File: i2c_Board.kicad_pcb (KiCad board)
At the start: 2 copper layers, 47.3 x 38 mm, 23 parts, among them J1 Conn_01x09_Pin, J2 Logic Analyzer Connector Pins, U1 MCP9808, U2 MCP7940N, Y1 Crystal

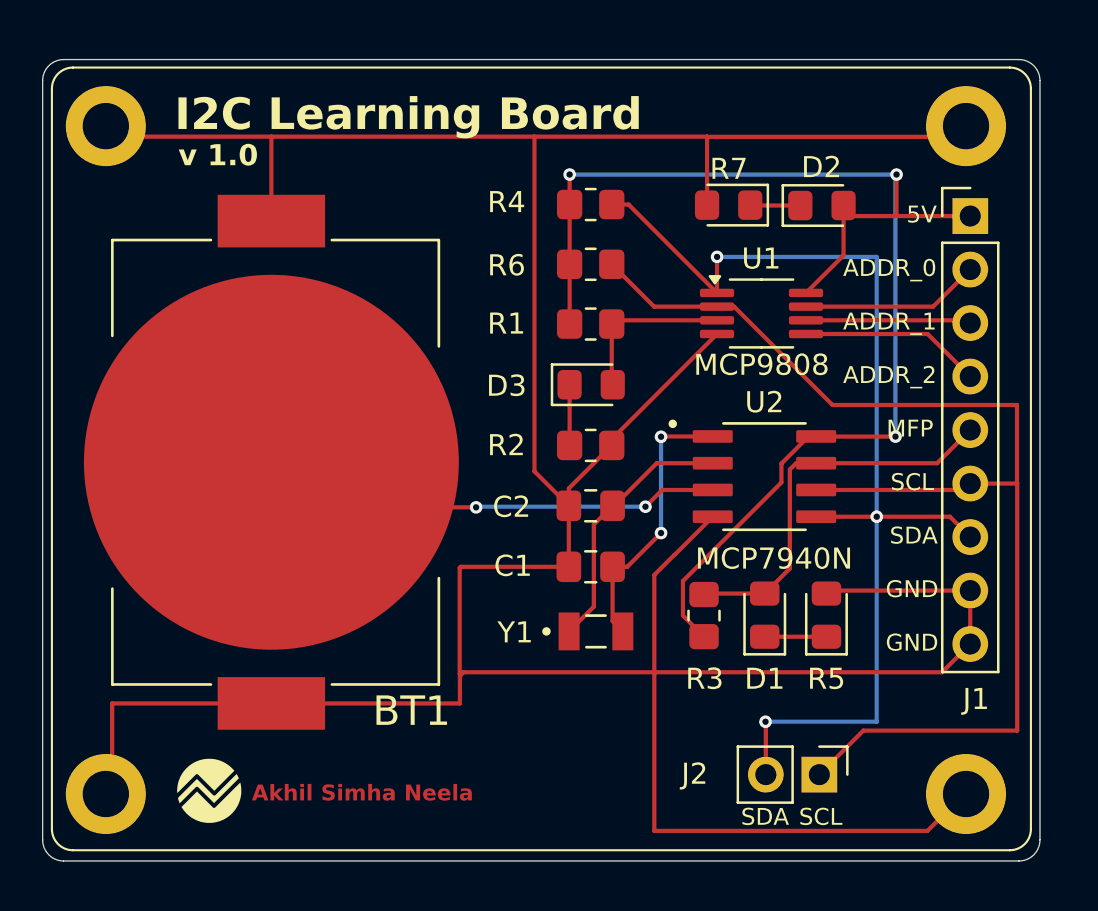
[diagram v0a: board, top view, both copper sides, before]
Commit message: Modified footprint & Rearranged routing
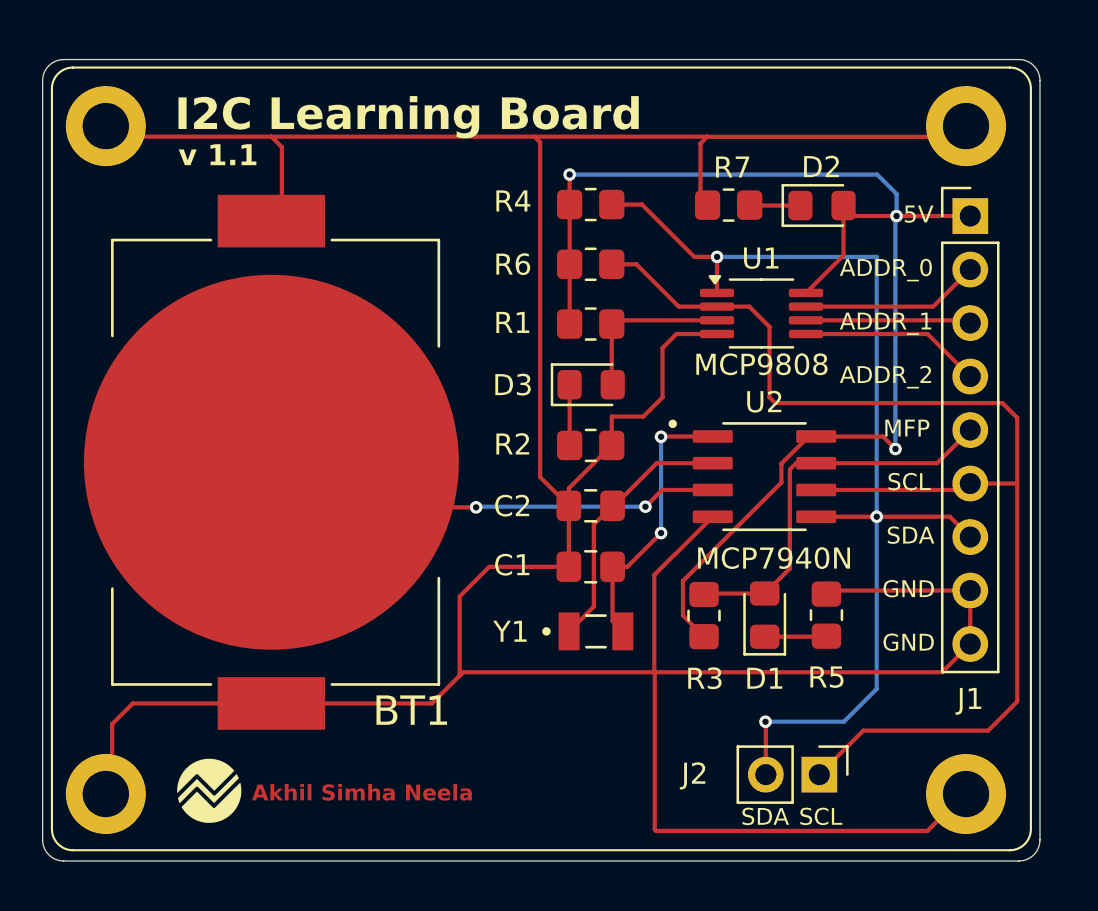
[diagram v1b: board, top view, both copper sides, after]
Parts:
- R5, R7: footprint Diode_SMD:D_0805_2012Metric_Pad1.15x1.40mm_HandSolder -> Resistor_SMD:R_0805_2012Metric_Pad1.20x1.40mm_HandSolder
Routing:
- net +5V: track 64.7 -> 63.0 mm
- net MCU_SDA: track 53.6 -> 52.0 mm
- net MCU_SCL: track 57.4 -> 58.2 mm
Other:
- board text added: "v 1.1"
- board text removed: "v 1.0"

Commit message: Changed Capacitor value from 6nF to 6pF
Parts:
- C1, C2: value 6n -> 6p
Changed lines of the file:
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@@
 			)
 		)
-		(property "Value" "6n"
+		(property "Value" "6p"
 			(at 0 1.68 0)
 			(layer "F.Fab")
@@
 			)
 		)
-		(property "Value" "6n"
+		(property "Value" "6p"
 			(at 0 1.68 0)
 			(layer "F.Fab")

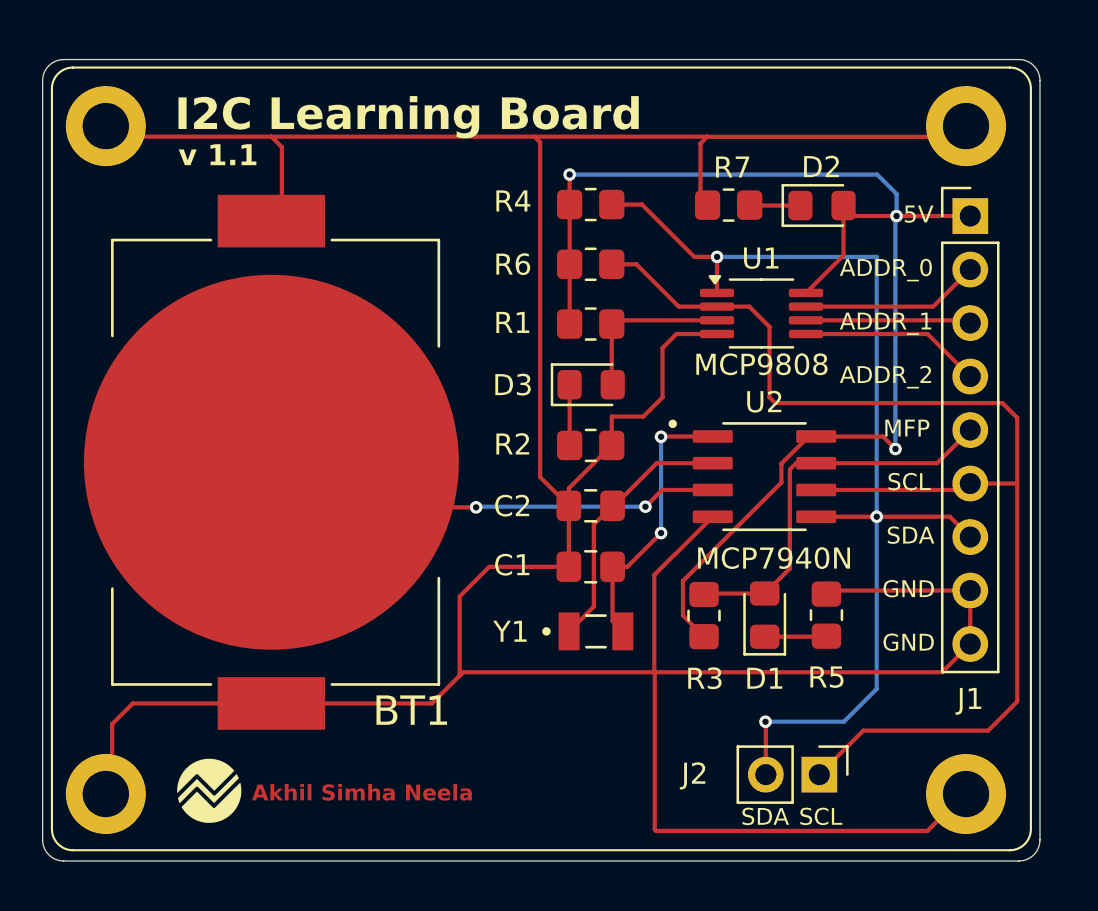
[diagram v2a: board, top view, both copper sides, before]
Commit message: Optimised board to smaller size & Added Ground Plane
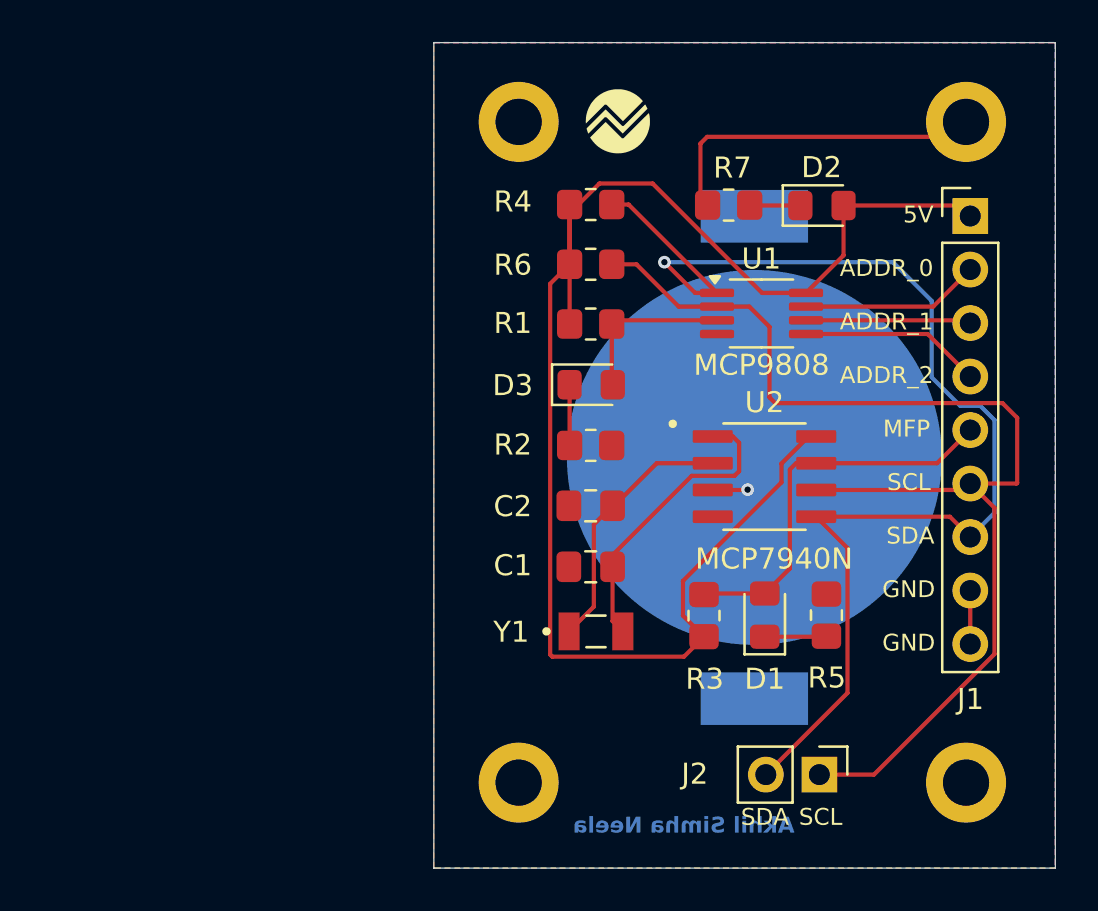
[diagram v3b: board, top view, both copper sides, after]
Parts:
- BT1: moved to B.Cu
- moved G*** 37.2 mm to (146.5, 75.9)
- moved BT1 22.9 mm to (152.9, 91.9)
- moved H4 19.6 mm to (141.8, 107.3)
- moved H1 19.6 mm to (141.8, 76.0)
- moved H3 0.54 mm to (163.0, 107.3)
- moved H2 0.20 mm to (163.0, 76.0)
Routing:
- net GND: track 179.4 -> 18.7 mm
- net Net-(U2-VBAT): track 22.2 -> 1.66 mm, vias 2 -> 1
- net +5V: track 63.0 -> 72.6 mm, vias 3 -> 0
- net MCU_SDA: track 52.0 -> 59.0 mm, vias 3 -> 1
- net MCU_SCL: track 58.2 -> 56.3 mm
- net Net-(U2-X1): track 13.3 -> 14.2 mm, vias 2 -> 0
- added copper zone on B.Cu, net GND
- added copper zone on F.Cu, net GND
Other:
- board size 47.3 x 38 mm -> 29.5 x 39.2 mm
